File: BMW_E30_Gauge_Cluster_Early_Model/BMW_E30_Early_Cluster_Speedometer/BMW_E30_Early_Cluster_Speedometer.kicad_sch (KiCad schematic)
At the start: 0 parts

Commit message: Added Library for custom symbols
Added the UAF2115 speedometer driver IC symbol
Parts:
- added U1: UAF2115, symbol BMW_ICs:UAF2115
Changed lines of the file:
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@@
 	(generator_version "9.0")
 	(paper "A4")
+	(symbol
+		(lib_id "BMW_ICs:UAF2115")
+		(at 144.78 88.9 0)
+		(unit 1)
+		(exclude_from_sim no)
+		(in_bom yes)
+		(on_board yes)
+		(dnp no)
+		(fields_autoplaced yes)
+		(property "Reference" "U1"
+			(at 146.9233 73.66 0)
+			(effects
+				(font
+					(size 1.27 1.27)
+				)
+				(justify left)
+			)
+		)
+		(property "Value" "UAF2115"
+			(at 146.9233 76.2 0)
+			(effects
+				(font
+					(size 1.27 1.27)
+				)
+				(justify left)
+			)
+		)
+		(property "Footprint" ""
+			(at 144.78 88.9 0)
+			(effects
+				(font
+					(size 1.27 1.27)
+				)
+				(hide yes)
+			)
+		)
+		(property "Datasheet" ""
+			(at 144.78 88.9 0)
+			(effects
+				(font
+					(size 1.27 1.27)
+				)
+				(hide yes)
+			)
+		)
+		(property "Description" "Speedometer and Mileage Indicator"
+			(at 144.78 60.96 0)
+			(effects
+				(font
+					(size 1.27 1.27)
+				)
+				(hide yes)
+			)
+		)
+		(pin "7"
+		)
+		(pin "11"
+		)
+		(pin "10"
+		)
+		(pin "1"
+		)
+		(pin "2"
+		)
+		(pin "12"
+		)
+		(pin "3"
+		)
+		(pin "4"
+		)
+		(pin "5"
+		)
+		(pin "13"
+		)
+		(pin "6"
+		)
+		(pin "8"
+		)
+		(pin "9"
+		)
+		(instances
+			(project ""
+				(path "/9a835706-2a71-4b4d-aadf-5c5569044960"
+					(reference "U1")
+					(unit 1)
+				)
+			)
+		)
+	)
 	(sheet_instances
 		(path "/"

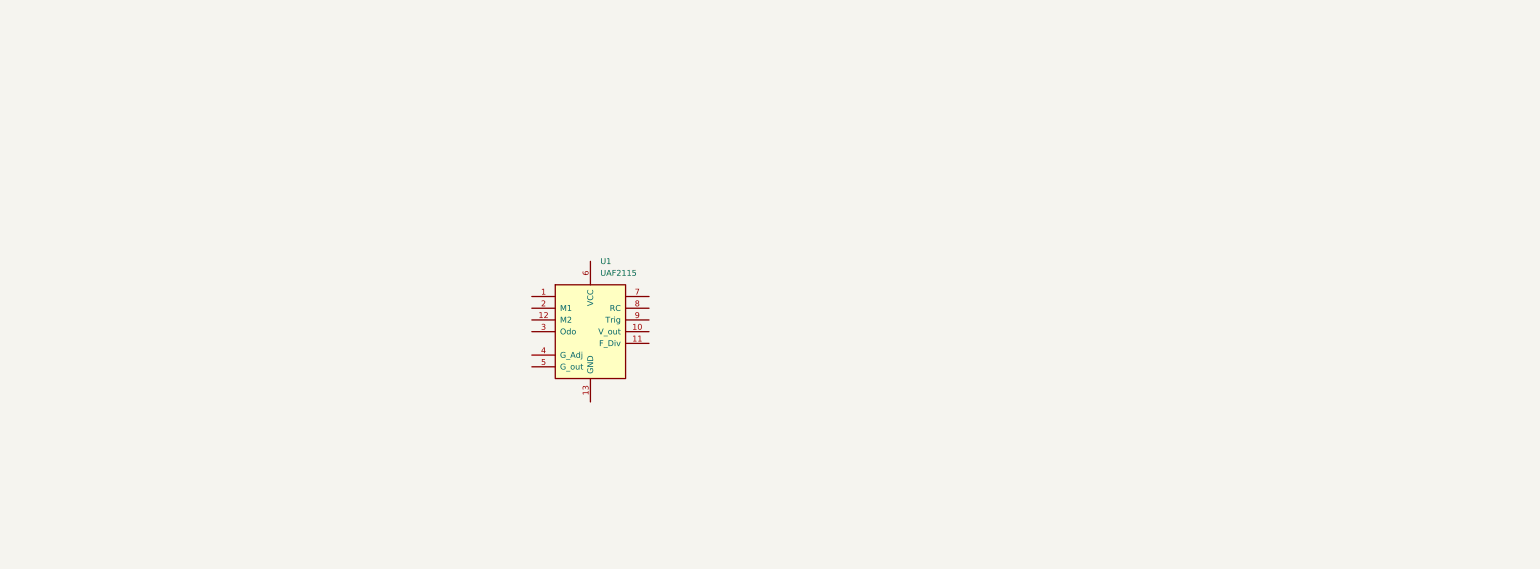
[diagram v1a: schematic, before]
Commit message: Created Schematic for Speedometer Board
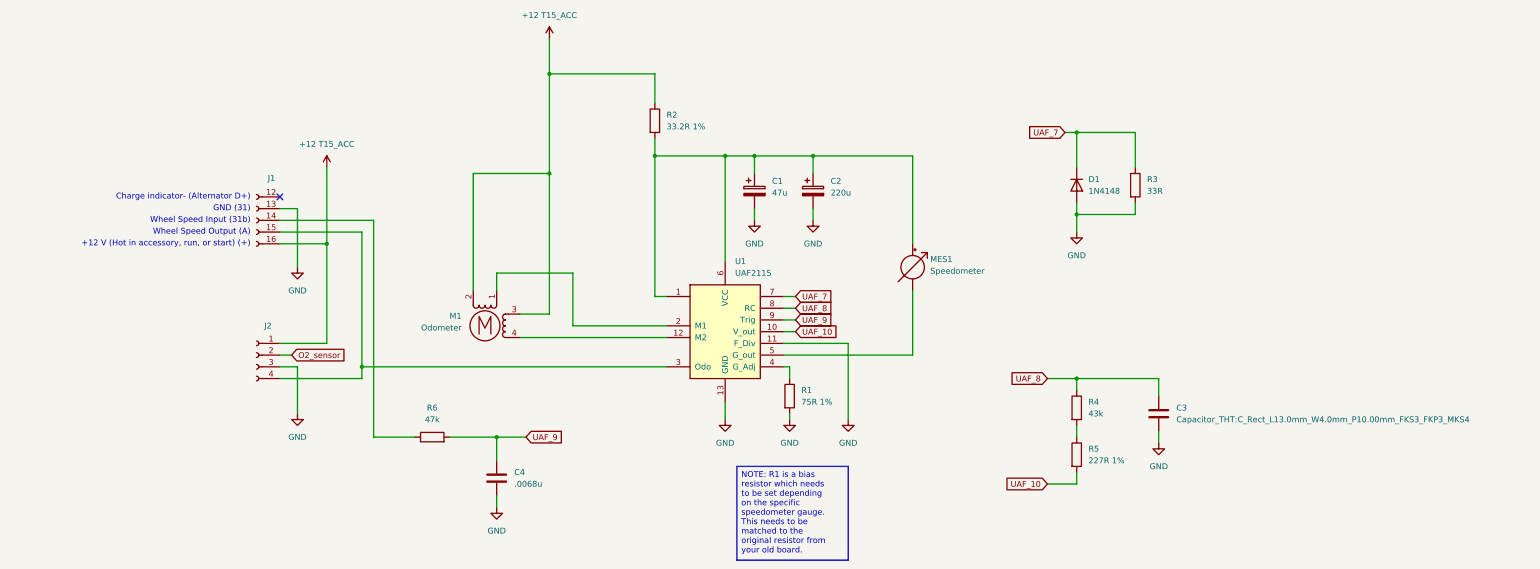
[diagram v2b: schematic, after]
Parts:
- added C1: 47u, Capacitor_THT:CP_Radial_D6.3mm_P2.50mm, symbol Device:C_Polarized
- added C2: 220u, Capacitor_THT:CP_Radial_D10.0mm_P5.00mm, symbol Device:C_Polarized
- added C3: Capacitor_THT:C_Rect_L13.0mm_W4.0mm_P10.00mm_FKS3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, symbol Device:C
- added C4: .0068u, Capacitor_THT:C_Rect_L13.0mm_W4.0mm_P10.00mm_FKS3_FKP3_MKS4, symbol Device:C
- added D1: 1N4148, Diode_THT:D_DO-35_SOD27_P10.16mm_Horizontal, symbol Diode:1N4148
- added J1: Conn_01x06_Socket, symbol Connector:Conn_01x05_Socket
- added J2: Conn_01x04_Socket, symbol Connector:Conn_01x04_Socket
- added M1: Odometer, symbol Motor:Stepper_Motor_bipolar
- added MES1: Speedometer, symbol Device:Galvanometer
- added R1: 75R 1%, Resistor_THT:R_Axial_DIN0207_L6.3mm_D2.5mm_P10.16mm_Horizontal, symbol Device:R
- added R2: 33.2R 1%, Resistor_THT:R_Axial_DIN0207_L6.3mm_D2.5mm_P10.16mm_Horizontal, symbol Device:R
- added R3: 33R, Resistor_THT:R_Axial_DIN0207_L6.3mm_D2.5mm_P10.16mm_Horizontal, symbol Device:R
- added R4: 43k, Resistor_THT:R_Axial_DIN0207_L6.3mm_D2.5mm_P10.16mm_Horizontal, symbol Device:R
- added R5: 227R 1%, Resistor_THT:R_Axial_DIN0207_L6.3mm_D2.5mm_P10.16mm_Horizontal, symbol Device:R
- added R6: 47k, Resistor_THT:R_Axial_DIN0207_L6.3mm_D2.5mm_P10.16mm_Horizontal, symbol Device:R
- U1: footprint (none) -> BMW_ICs:UAF2115
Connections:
- net at U1.1: now also U1.6 (VCC), C1.1, C2.1, MES1.2 (+), R2.2
- net UAF_10: now reaches U1.10 (V_out)
- net UAF_10: now also R5.2
- net GND: now reaches U1.11 (F_Div)
- net GND: now also U1.13 (GND), C1.2, C2.2, C3.2, C4.2, D1.2 (A), J1.13 (Pin_2), J2.3 (Pin_3), R1.2, R3.2
- net at U1.12 (M2): now also M1.4
- net at U1.2 (M1): now also M1.1
- net at U1.3 (Odo): now also J1.15 (Pin_4), J2.4 (Pin_4)
- net at U1.4 (G_Adj): now also R1.1
- net at U1.5 (G_out): now also MES1.1 (-)
- net UAF_7: now reaches U1.7
- net UAF_7: now also D1.1 (K), R3.1
- net UAF_8: now reaches U1.8 (RC)
- net UAF_8: now also C3.1, R4.1
- net UAF_9: now reaches U1.9 (Trig)
- net UAF_9: now also C4.1, R6.2
- new net: R4.2, R5.1
- new net: J1.14 (Pin_3), R6.1
- new net +12 T15_ACC: J1.16 (Pin_5), J2.1 (Pin_1), M1.2 (-), M1.3, R2.1
- new net O2_sensor: J2.2 (Pin_2)
- no-connect marks 0 -> 1
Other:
- note added: "+12 V (Hot in accessory, run, or start) (+)"
- note added: "Charge indicator- (Alternator D+)"
- note added: "GND (31)"
- note added: "Wheel Speed Input (31b)"
- note added: "Wheel Speed Output (A)"
- title: (none) -> BMW E30 Speedometer Driver
- moved on the sheet: U1

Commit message: Speedometer PCB Started
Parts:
- C3: value Capacitor_THT:C_Rect_L13.0mm_W4.0mm_P10.00mm_FKS3_FKP3_MKS4 -> .047u; footprint (none) -> Capacitor_THT:C_Rect_L13.0mm_W4.0mm_P10.00mm_FKS3_FKP3_MKS4
- J1: footprint (none) -> BMW_Cluster_Connectors:Connector_Speedometer
- J2: now not fitted
- M1: footprint (none) -> BMW_Cluster_Connectors:Odometer_Stepper
- MES1: footprint (none) -> BMW_Cluster_Connectors:Speedometer_Galvanometer
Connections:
- net +12 T15_ACC: no longer M1.2 (-)
- net at U1.12 (M2): now also M1.2; no longer M1.4
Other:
- company: (none) -> Reagan Ansel
- title: BMW E30 Speedometer Driver -> BMW E30 Speedometer Driver Schematic
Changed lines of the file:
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@@
 	(paper "A4")
 	(title_block
-		(title "BMW E30 Speedometer Driver")
+		(title "BMW E30 Speedometer Driver Schematic")
+		(company "Reagan Ansel")
 	)
 	(text "+12 V (Hot in accessory, run, or start) (+)"
@@
 			)
 		)
-		(property "Footprint" ""
+		(property "Footprint" "BMW_Cluster_Connectors:Speedometer_Galvanometer"
 			(at 214.63 72.39 90)
 			(effects
@@
 		(in_bom yes)
 		(on_board yes)
-		(dnp no)
+		(dnp yes)
 		(property "Reference" "J2"
 			(at 75.692 87.63 0)
@@
 			)
 		)
-		(property "Value" "Capacitor_THT:C_Rect_L13.0mm_W4.0mm_P10.00mm_FKS3_FKP3_MKS4"
+		(property "Value" ".047u"
 			(at 271.78 107.9499 0)
 			(effects
@@
 			)
 		)
-		(property "Footprint" ""
+		(property "Footprint" "Capacitor_THT:C_Rect_L13.0mm_W4.0mm_P10.00mm_FKS3_FKP3_MKS4"
 			(at 268.9352 110.49 0)
 			(effects
@@
 			)
 		)
-		(property "Footprint" ""
+		(property "Footprint" "BMW_Cluster_Connectors:Odometer_Stepper"
 			(at 121.666 87.884 0)
 			(effects
@@
 			)
 		)
-		(property "Datasheet" "http://www.infineon.com/dgdl/Application-Note-TLE8110EE_driving_UniPolarStepperMotor_V1.1.pdf?fileId=db3a30431be39b97011be5d0aa0a00b0"
+		(property "Datasheet" ""
 			(at 121.666 87.884 0)
 			(effects
@@
 			)
 		)
-		(property "Description" "4-wire bipolar stepper motor"
+		(property "Description" "Odometer Stepper Motor"
 			(at 121.92 87.63 0)
 			(effects
@@
 		(pin "1"
 		)
-		(pin "4"
+		(pin "3"
 		)
 		(pin "2"
@@
 			)
 		)
-		(property "Footprint" ""
+		(property "Footprint" "BMW_Cluster_Connectors:Connector_Speedometer"
 			(at 72.39 64.77 0)
 			(effects

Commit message: Schematic Correction & Resources
Corrected an error in the schematic and also added in a resources folder containing the datasheet for the SAF2115 chip on the board.
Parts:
- J2: now fitted
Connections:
- net GND: no longer R3.2
- net at J1.14 (Pin_3), R6.1: now also R3.2
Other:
- moved on the sheet: D1, R3
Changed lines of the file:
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@@
+	)
+	(junction
+		(at 97.79 138.43)
+		(diameter 0)
+		(color 0 0 0 0)
 	)
 	(junction
@@
 	)
 	(junction
+		(at 97.79 111.76)
+		(diameter 0)
+		(color 0 0 0 0)
+	)
+	(junction
 		(at 95.25 96.52)
 		(diameter 0)
@@
 	)
 	(junction
-		(at 250.19 45.72)
-		(diameter 0)
-		(color 0 0 0 0)
-	)
-	(junction
 		(at 124.46 111.76)
 		(diameter 0)
@@
 		(color 0 0 0 0)
 	)
-	(junction
-		(at 250.19 63.5)
-		(diameter 0)
-		(color 0 0 0 0)
-	)
 	(no_connect
 		(at 77.47 59.69)
@@
 	(wire
 		(pts
-			(xy 262.89 53.34) (xy 262.89 45.72)
+			(xy 97.79 129.54) (xy 97.79 138.43)
 		)
 		(stroke
@@
 	(wire
 		(pts
+			(xy 97.79 111.76) (xy 97.79 121.92)
+		)
+		(stroke
+			(width 0)
+			(type default)
+		)
+	)
+	(wire
+		(pts
 			(xy 129.54 85.09) (xy 135.89 85.09)
 		)
@@
 	(wire
 		(pts
-			(xy 250.19 60.96) (xy 250.19 63.5)
-		)
-		(stroke
-			(width 0)
-			(type default)
-		)
-	)
-	(wire
-		(pts
 			(xy 95.25 67.31) (xy 77.47 67.31)
 		)
@@
 	(wire
 		(pts
-			(xy 247.65 45.72) (xy 250.19 45.72)
-		)
-		(stroke
-			(width 0)
-			(type default)
-		)
-	)
-	(wire
-		(pts
-			(xy 250.19 63.5) (xy 250.19 67.31)
+			(xy 114.3 138.43) (xy 97.79 138.43)
+		)
+		(stroke
+			(width 0)
+			(type default)
+		)
+	)
+	(wire
+		(pts
+			(xy 97.79 153.67) (xy 97.79 160.02)
 		)
 		(stroke
@@
 	(wire
 		(pts
-			(xy 262.89 60.96) (xy 262.89 63.5)
-		)
-		(stroke
-			(width 0)
-			(type default)
-		)
-	)
-	(wire
-		(pts
 			(xy 180.34 62.23) (xy 180.34 64.77)
 		)
@@
 	(wire
 		(pts
-			(xy 250.19 45.72) (xy 250.19 53.34)
+			(xy 97.79 138.43) (xy 97.79 146.05)
 		)
 		(stroke
@@
 	(wire
 		(pts
-			(xy 262.89 45.72) (xy 250.19 45.72)
-		)
-		(stroke
-			(width 0)
-			(type default)
-		)
-	)
-	(wire
-		(pts
 			(xy 158.75 39.37) (xy 158.75 33.02)
 		)
@@
 		(pts
 			(xy 124.46 111.76) (xy 130.81 111.76)
-		)
-		(stroke
-			(width 0)
-			(type default)
-		)
-	)
-	(wire
-		(pts
-			(xy 262.89 63.5) (xy 250.19 63.5)
 		)
 		(stroke
@@
 	(global_label "UAF_7"
 		(shape input)
-		(at 247.65 45.72 180)
+		(at 114.3 138.43 0)
 		(fields_autoplaced yes)
 		(effects
@@
 				(size 1.27 1.27)
 			)
-			(justify right)
+			(justify left)
 		)
 		(property "Intersheetrefs" "${INTERSHEET_REFS}"
-			(at 238.98 45.72 0)
-			(effects
-				(font
-					(size 1.27 1.27)
-				)
-				(justify right)
+			(at 122.97 138.43 0)
+			(effects
+				(font
+					(size 1.27 1.27)
+				)
+				(justify left)
 				(hide yes)
 			)
@@
 	(symbol
 		(lib_id "Diode:1N4148")
-		(at 250.19 57.15 270)
+		(at 97.79 149.86 270)
 		(unit 1)
 		(exclude_from_sim no)
@@
 		(fields_autoplaced yes)
 		(property "Reference" "D1"
-			(at 252.73 55.8799 90)
+			(at 100.33 148.5899 90)
 			(effects
 				(font
@@
 		)
 		(property "Value" "1N4148"
-			(at 252.73 58.4199 90)
+			(at 100.33 151.1299 90)
 			(effects
 				(font
@@
 		)
 		(property "Footprint" "Diode_THT:D_DO-35_SOD27_P10.16mm_Horizontal"
-			(at 250.19 57.15 0)
+			(at 97.79 149.86 0)
 			(effects
 				(font
@@
 		)
 		(property "Datasheet" "https://assets.nexperia.com/documents/data-sheet/1N4148_1N4448.pdf"
-			(at 250.19 57.15 0)
+			(at 97.79 149.86 0)
 			(effects
 				(font
@@
 		)
 		(property "Description" "100V 0.15A standard switching diode, DO-35"
-			(at 250.19 57.15 0)
+			(at 97.79 149.86 0)
 			(effects
 				(font
@@
 		)
 		(property "Sim.Device" "D"
-			(at 250.19 57.15 0)
+			(at 97.79 149.86 0)
 			(effects
 				(font
@@
 		)
 		(property "Sim.Pins" "1=K 2=A"
-			(at 250.19 57.15 0)
+			(at 97.79 149.86 0)
 			(effects
 				(font
@@
 		(in_bom yes)
 		(on_board yes)
-		(dnp yes)
+		(dnp no)
 		(property "Reference" "J2"
 			(at 75.692 87.63 0)
@@
 	(symbol
 		(lib_id "power:GND")
-		(at 250.19 67.31 0)
+		(at 97.79 160.02 0)
 		(unit 1)
 		(exclude_from_sim no)
@@
 		(fields_autoplaced yes)
 		(property "Reference" "#PWR09"
-			(at 250.19 73.66 0)
+			(at 97.79 166.37 0)
 			(effects
 				(font
@@
 		)
 		(property "Value" "GND"
-			(at 250.19 72.39 0)
+			(at 97.79 165.1 0)
 			(effects
 				(font
@@
 		)
 		(property "Footprint" ""
-			(at 250.19 67.31 0)
+			(at 97.79 160.02 0)
 			(effects
 				(font
@@
 		)
 		(property "Datasheet" ""
-			(at 250.19 67.31 0)
+			(at 97.79 160.02 0)
 			(effects
 				(font
@@
 		)
 		(property "Description" "Power symbol creates a global label with name \"GND\" , ground"
-			(at 250.19 67.31 0)
+			(at 97.79 160.02 0)
 			(effects
 				(font
@@
 	(symbol
 		(lib_id "Device:R")
-		(at 262.89 57.15 0)
+		(at 97.79 125.73 180)
 		(unit 1)
 		(exclude_from_sim no)
@@
 		(on_board yes)
 		(dnp no)
-		(fields_autoplaced yes)
 		(property "Reference" "R3"
-			(at 265.43 55.8799 0)
+			(at 95.25 127.0001 0)
 			(effects
 				(font
@@
 		)
 		(property "Value" "33R"
-			(at 265.43 58.4199 0)
+			(at 95.25 124.4601 0)
 			(effects
 				(font
@@
 		)
 		(property "Footprint" "Resistor_THT:R_Axial_DIN0207_L6.3mm_D2.5mm_P10.16mm_Horizontal"
-			(at 261.112 57.15 90)
+			(at 99.568 125.73 90)
 			(effects
 				(font
@@
 		)
 		(property "Datasheet" "~"
-			(at 262.89 57.15 0)
+			(at 97.79 125.73 0)
 			(effects
 				(font
@@
 		)
 		(property "Description" "Resistor"
-			(at 262.89 57.15 0)
-			(effects
-				(font
+			(at 97.79 125.73 0)
+			(effects
+				(font

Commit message: Layout Updates
Drew out board cut outlines and 2 clearance holes for the speedometer mounts. Added footprint for O2 sensor connector as well.
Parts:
- J2: footprint (none) -> BMW_Cluster_Connectors:BMW_1372218
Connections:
- net +12 T15_ACC: now also M1.2 (-); no longer M1.3 (-)
- net at U1.12 (M2): now also M1.3; no longer M1.2
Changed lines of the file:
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@@
 			)
 		)
-		(property "Footprint" ""
+		(property "Footprint" "BMW_Cluster_Connectors:BMW_1372218"
 			(at 72.39 93.98 0)
 			(effects
@@
 		(pin "2"
 		)
-		(pin "3"
-		)
-		(instances
+		(pin "2"
+		)
+		(instances

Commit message: Schematic Updates
Progress on full speedometer schematic
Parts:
- added C5: 100u, Capacitor_THT:CP_Radial_D10.0mm_P5.00mm, symbol Device:C_Polarized
- added C6: ?, Capacitor_THT:CP_Radial_D10.0mm_P5.00mm, symbol Device:C_Polarized
- added D2: 1N4005, Diode_THT:D_DO-41_SOD81_P10.16mm_Horizontal, symbol Diode:1N4005
- added R7: 30R, Resistor_THT:R_Axial_DIN0207_L6.3mm_D2.5mm_P10.16mm_Horizontal, symbol Device:R
- added U2: UGS 3020, Package_TO_SOT_THT:TO-92S, symbol Sensor_Magnetic:A1302xUA
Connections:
- net +12 T15_ACC: now also D2.2 (A)
- net GND: now also C5.2, C6.2
- net D+: now reaches J1.12 (Pin_1)
- new net: C5.1, C6.1, R7.2
- new net T15_Protected: D2.1 (K), R7.1, U2.1 (V_{CC})
- no-connect marks 1 -> 0
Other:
- moved on the sheet: C1, C2, C3, C4, D1, J1, J2, M1, MES1, R1, R2, R3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

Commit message: Completed Schematic Diagram of Speedometer
Make sure to verify schematic during layout with the reference board.
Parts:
- added C7: 0.47u, Capacitor_THT:C_Rect_L13.0mm_W4.0mm_P10.00mm_FKS3_FKP3_MKS4, symbol Device:C
- added C8: 47u, Capacitor_THT:CP_Radial_D6.3mm_P2.50mm, symbol Device:C_Polarized
- added D3: 1N4148, Diode_THT:D_DO-35_SOD27_P10.16mm_Horizontal, symbol Diode:1N4148
- added D4, D5: 1N4005, Diode_THT:D_DO-41_SOD81_P10.16mm_Horizontal, symbol Diode:1N4005
- added D6: D_Zener, symbol Device:D_Zener
- added F1: Fuse, symbol Device:Fuse
- added Q1: BC327-40, Package_TO_SOT_THT:TO-92_Inline, symbol Transistor_BJT:BC327
- added Q2: BD135, Package_TO_SOT_THT:TO-126-3_Vertical, symbol Transistor_BJT:BD135
- added R10: 10R, Resistor_THT:R_Axial_DIN0207_L6.3mm_D2.5mm_P10.16mm_Horizontal, symbol Device:R
- added R11: 330R, Resistor_THT:R_Axial_DIN0207_L6.3mm_D2.5mm_P10.16mm_Horizontal, symbol Device:R
- added R12: 10k, Resistor_THT:R_Axial_DIN0207_L6.3mm_D2.5mm_P10.16mm_Horizontal, symbol Device:R
- added R13: 47k, Resistor_THT:R_Axial_DIN0207_L6.3mm_D2.5mm_P10.16mm_Horizontal, symbol Device:R
- added R14: ?, Resistor_THT:R_Axial_DIN0207_L6.3mm_D2.5mm_P5.08mm_Vertical, symbol Device:R
- added R8: 510R?, Resistor_THT:R_Axial_DIN0207_L6.3mm_D2.5mm_P10.16mm_Horizontal, symbol Device:R
- added R9: 3k, Resistor_THT:R_Axial_DIN0207_L6.3mm_D2.5mm_P10.16mm_Horizontal, symbol Device:R
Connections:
- net D+: now also D5.1 (K)
- net GND: now also U2.2 (GND), C7.2, C8.2, D4.1 (K), D6.2 (A), F1.2, R12.1
- net O2_sensor: now also D5.2 (A), D6.1 (K), Q2.2 (C)
- net UAF_10: now also C7.1, R14.2
- net UAF_8: now also R14.1
- net UAF_9: now also R13.2
- net at C1.1, C2.1, MES1.2 (+)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: now also C8.1
- net at C5.1, C6.1, R7.2: now also Q1.3 (E), R11.2, R9.2
- net at U2.3 (V_{OUT}): now also R8.2
- net at J1.14 (Pin_3), R3.2, R6.1: now also R13.1
- new net: D4.2 (A), Q2.1 (E)
- new net: D3.2 (A), Q2.3 (B), R11.1, R12.2
- new net: D3.1 (K), F1.1, R10.1
- new net: Q1.1 (C), R10.2
- new net: Q1.2 (B), R8.1, R9.1
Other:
- moved on the sheet: C3, C5, C6, D2, MES1, R7, U2

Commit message: Component Layout
Rough layout of components completed
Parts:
- C7: footprint Capacitor_THT:C_Rect_L13.0mm_W4.0mm_P10.00mm_FKS3_FKP3_MKS4 -> Capacitor_THT:C_Disc_D7.5mm_W2.5mm_P5.00mm
- D6: footprint (none) -> Diode_THT:D_DO-35_SOD27_P10.16mm_Horizontal
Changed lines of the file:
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@@
 			)
 		)
-		(property "Footprint" "Capacitor_THT:C_Rect_L13.0mm_W4.0mm_P10.00mm_FKS3_FKP3_MKS4"
+		(property "Footprint" "Capacitor_THT:C_Disc_D7.5mm_W2.5mm_P5.00mm"
 			(at 53.0352 134.62 0)
 			(effects
@@
 			)
 		)
-		(property "Footprint" ""
+		(property "Footprint" "Diode_THT:D_DO-35_SOD27_P10.16mm_Horizontal"
 			(at 381 196.85 0)
 			(effects
